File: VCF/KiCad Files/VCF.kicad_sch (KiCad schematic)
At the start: 64 parts, among them J1 AUDIO_IN, J2 CV1, J3 CV2, J4 AUDIO_OUT, J5 Conn_02x05_Odd_Even, J6 Conn_01x05_Male, J7 Conn_01x05_Female, J8 Conn_01x08_Male, J9 Conn_01x08_Female, SW1 SW_DPDT_x2, U1 TL074, U2 TL074

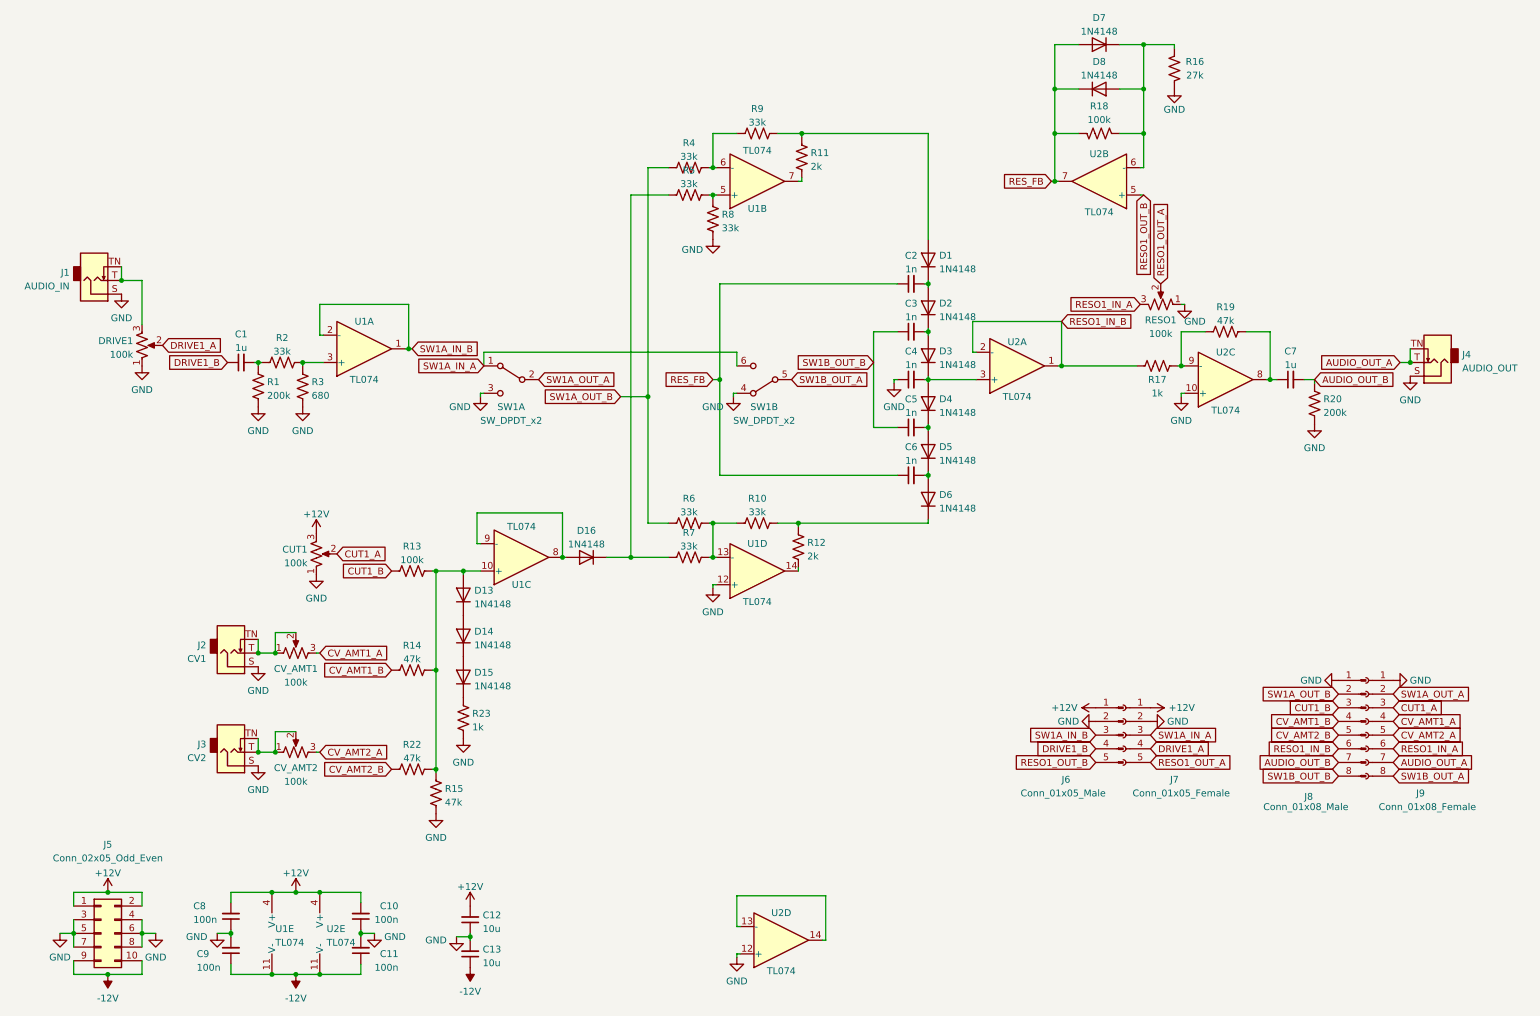
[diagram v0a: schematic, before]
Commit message: Corrected PCB
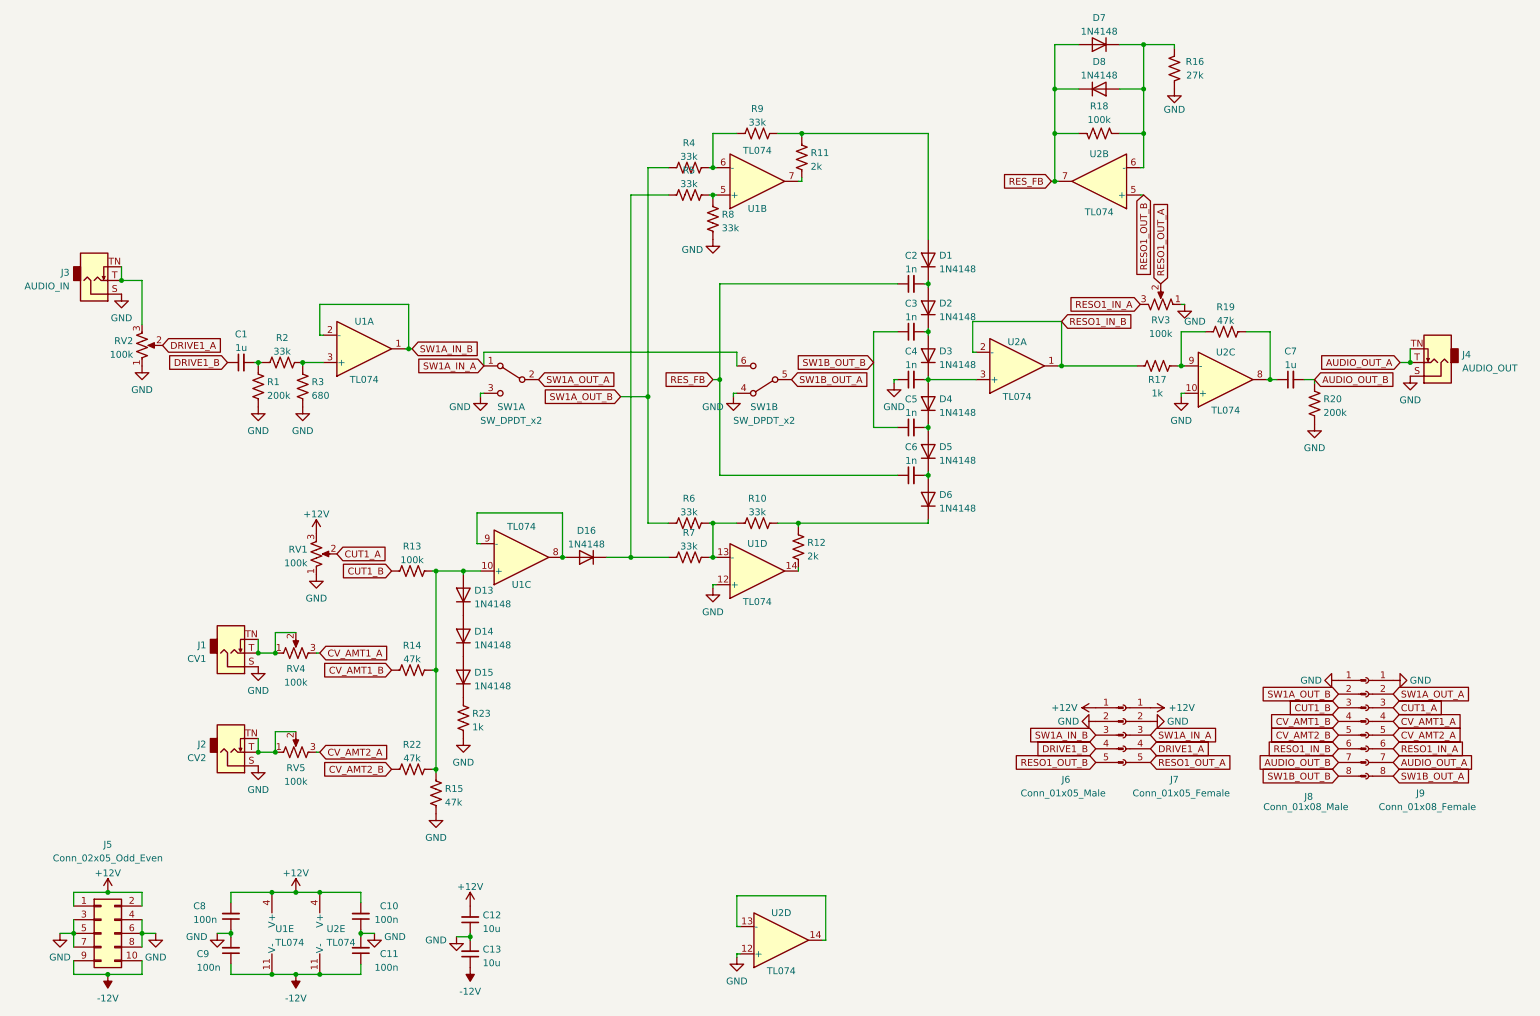
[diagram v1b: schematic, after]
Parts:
- renumbered J2 to J1, J3 to J2, J1 to J3, CUT1 to RV1, DRIVE1 to RV2, RESO1 to RV3, CV_AMT1 to RV4, CV_AMT2 to RV5
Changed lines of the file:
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@@
   (symbol (lib_id "Device:R_Potentiometer_US") (at 30.48 74.295 0) (mirror x) (unit 1)
     (in_bom yes) (on_board yes)
-    (property "Reference" "DRIVE1" (id 0) (at 28.829 73.4603 0)
+    (property "Reference" "RV2" (id 0) (at 28.829 73.4603 0)
       (effects (font (size 1.27 1.27)) (justify right))
     )
@@
   (symbol (lib_id "Device:R_Potentiometer_US") (at 62.865 113.03 0) (mirror x) (unit 1)
     (in_bom yes) (on_board yes) (fields_autoplaced)
-    (property "Reference" "CUT1" (id 0) (at 61.214 112.1953 0)
-      (effects (font (size 1.27 1.27)) (justify right))
-    )
-    (property "Value" "100k" (id 1) (at 61.214 114.7322 0)
+    (property "Reference" "RV1" (id 0) (at 61.2141 112.1953 0)
+      (effects (font (size 1.27 1.27)) (justify right))
+    )
+    (property "Value" "100k" (id 1) (at 61.2141 114.7322 0)
       (effects (font (size 1.27 1.27)) (justify right))
     )
@@
   (symbol (lib_id "Connector:AudioJack2_SwitchT") (at 21.59 62.23 0) (mirror x) (unit 1)
     (in_bom yes) (on_board yes) (fields_autoplaced)
-    (property "Reference" "J1" (id 0) (at 17.0181 60.7603 0)
+    (property "Reference" "J3" (id 0) (at 17.0181 60.7603 0)
       (effects (font (size 1.27 1.27)) (justify right))
     )
@@
   (symbol (lib_id "Device:R_Potentiometer_US") (at 59.055 149.86 90) (unit 1)
     (in_bom yes) (on_board yes) (fields_autoplaced)
-    (property "Reference" "CV_AMT2" (id 0) (at 59.055 152.7794 90))
+    (property "Reference" "RV5" (id 0) (at 59.055 152.7794 90))
     (property "Value" "100k" (id 1) (at 59.055 155.3163 90))
     (property "Footprint" "1_CUSTOM:Potentiometer_Alpha_Metal" (id 2) (at 59.055 149.86 0)
@@
   (symbol (lib_id "Device:R_Potentiometer_US") (at 219.71 66.675 270) (mirror x) (unit 1)
     (in_bom yes) (on_board yes) (fields_autoplaced)
-    (property "Reference" "RESO1" (id 0) (at 219.71 69.5944 90))
+    (property "Reference" "RV3" (id 0) (at 219.71 69.5944 90))
     (property "Value" "100k" (id 1) (at 219.71 72.1313 90))
     (property "Footprint" "1_CUSTOM:Potentiometer_Alpha_Metal" (id 2) (at 219.71 66.675 0)
@@
   (symbol (lib_id "Connector:AudioJack2_SwitchT") (at 46.99 149.86 0) (mirror x) (unit 1)
     (in_bom yes) (on_board yes) (fields_autoplaced)
-    (property "Reference" "J3" (id 0) (at 42.4181 148.3903 0)
+    (property "Reference" "J2" (id 0) (at 42.4181 148.3903 0)
       (effects (font (size 1.27 1.27)) (justify right))
     )
@@
   (symbol (lib_id "Connector:AudioJack2_SwitchT") (at 46.99 131.445 0) (mirror x) (unit 1)
     (in_bom yes) (on_board yes) (fields_autoplaced)
-    (property "Reference" "J2" (id 0) (at 42.4181 129.9753 0)
+    (property "Reference" "J1" (id 0) (at 42.4181 129.9753 0)
       (effects (font (size 1.27 1.27)) (justify right))
     )
@@
   (symbol (lib_id "Device:R_Potentiometer_US") (at 59.055 131.445 90) (unit 1)
     (in_bom yes) (on_board yes) (fields_autoplaced)
-    (property "Reference" "CV_AMT1" (id 0) (at 59.055 134.3644 90))
+    (property "Reference" "RV4" (id 0) (at 59.055 134.3644 90))
     (property "Value" "100k" (id 1) (at 59.055 136.9013 90))
     (property "Footprint" "1_CUSTOM:Potentiometer_Alpha_Metal" (id 2) (at 59.055 131.445 0)
@@
       (reference "C13") (unit 1) (value "10u") (footprint "Capacitor_SMD:CP_Elec_5x5.4")
     )
-    (path "/381f4c0d-9543-4911-8da2-34e065cd7bd2"
-      (reference "CUT1") (unit 1) (value "100k") (footprint "1_CUSTOM:Potentiometer_Alpha_Metal")
-    )
-    (path "/df147264-04c5-448c-aef7-d922329bd23c"
-      (reference "CV_AMT1") (unit 1) (value "100k") (footprint "1_CUSTOM:Potentiometer_Alpha_Metal")
-    )
-    (path "/709215a6-0e79-4071-81e0-fccd8f17331b"
-      (reference "CV_AMT2") (unit 1) (value "100k") (footprint "1_CUSTOM:Potentiometer_Alpha_Metal")
-    )
     (path "/5dde91f8-ddf6-45eb-a0db-b81980ac66ac"
       (reference "D1") (unit 1) (value "1N4148") (footprint "Diode_SMD:D_SOD-323_HandSoldering")
@@
       (reference "D16") (unit 1) (value "1N4148") (footprint "Diode_SMD:D_SOD-323_HandSoldering")
     )
-    (path "/2163dbd0-9c20-4f43-b9c8-b7932544841e"
-      (reference "DRIVE1") (unit 1) (value "100k") (footprint "1_CUSTOM:Potentiometer_Alpha_Metal")
+    (path "/cf157f36-01a1-4d50-b942-70f5c7e8db53"
+      (reference "J1") (unit 1) (value "CV1") (footprint "1_CUSTOM:Jack_3.5mm_QingPu_WQP-PJ398SM_Vertical_CircularHoles_Compact")
+    )
+    (path "/8e3c0888-34bb-466d-9c9f-31b726e28c32"
+      (reference "J2") (unit 1) (value "CV2") (footprint "1_CUSTOM:Jack_3.5mm_QingPu_WQP-PJ398SM_Vertical_CircularHoles_Compact")
     )
     (path "/5c1b3168-0f23-417d-aad7-0902d6085c21"
-      (reference "J1") (unit 1) (value "AUDIO_IN") (footprint "1_CUSTOM:Jack_3.5mm_QingPu_WQP-PJ398SM_Vertical_CircularHoles_Compact")
-    )
-    (path "/cf157f36-01a1-4d50-b942-70f5c7e8db53"
-      (reference "J2") (unit 1) (value "CV1") (footprint "1_CUSTOM:Jack_3.5mm_QingPu_WQP-PJ398SM_Vertical_CircularHoles_Compact")
-    )
-    (path "/8e3c0888-34bb-466d-9c9f-31b726e28c32"
-      (reference "J3") (unit 1) (value "CV2") (footprint "1_CUSTOM:Jack_3.5mm_QingPu_WQP-PJ398SM_Vertical_CircularHoles_Compact")
+      (reference "J3") (unit 1) (value "AUDIO_IN") (footprint "1_CUSTOM:Jack_3.5mm_QingPu_WQP-PJ398SM_Vertical_CircularHoles_Compact")
     )
     (path "/49ae8030-f3a5-42e5-a910-2db8c6cc87f3"
@@
       (reference "R23") (unit 1) (value "1k") (footprint "Resistor_SMD:R_0603_1608Metric_Pad0.98x0.95mm_HandSolder")
     )
+    (path "/381f4c0d-9543-4911-8da2-34e065cd7bd2"
+      (reference "RV1") (unit 1) (value "100k") (footprint "1_CUSTOM:Potentiometer_Alpha_Metal")
+    )
+    (path "/2163dbd0-9c20-4f43-b9c8-b7932544841e"
+      (reference "RV2") (unit 1) (value "100k") (footprint "1_CUSTOM:Potentiometer_Alpha_Metal")
+    )
     (path "/746d8b00-b8bf-43c7-aa7a-571bd4239b35"
-      (reference "RESO1") (unit 1) (value "100k") (footprint "1_CUSTOM:Potentiometer_Alpha_Metal")
+      (reference "RV3") (unit 1) (value "100k") (footprint "1_CUSTOM:Potentiometer_Alpha_Metal")
+    )
+    (path "/df147264-04c5-448c-aef7-d922329bd23c"
+      (reference "RV4") (unit 1) (value "100k") (footprint "1_CUSTOM:Potentiometer_Alpha_Metal")
+    )
+    (path "/709215a6-0e79-4071-81e0-fccd8f17331b"
+      (reference "RV5") (unit 1) (value "100k") (footprint "1_CUSTOM:Potentiometer_Alpha_Metal")
     )
     (path "/c2e3be15-ede1-4026-84c1-4e22811d1263"

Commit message: Cleaned up schematic
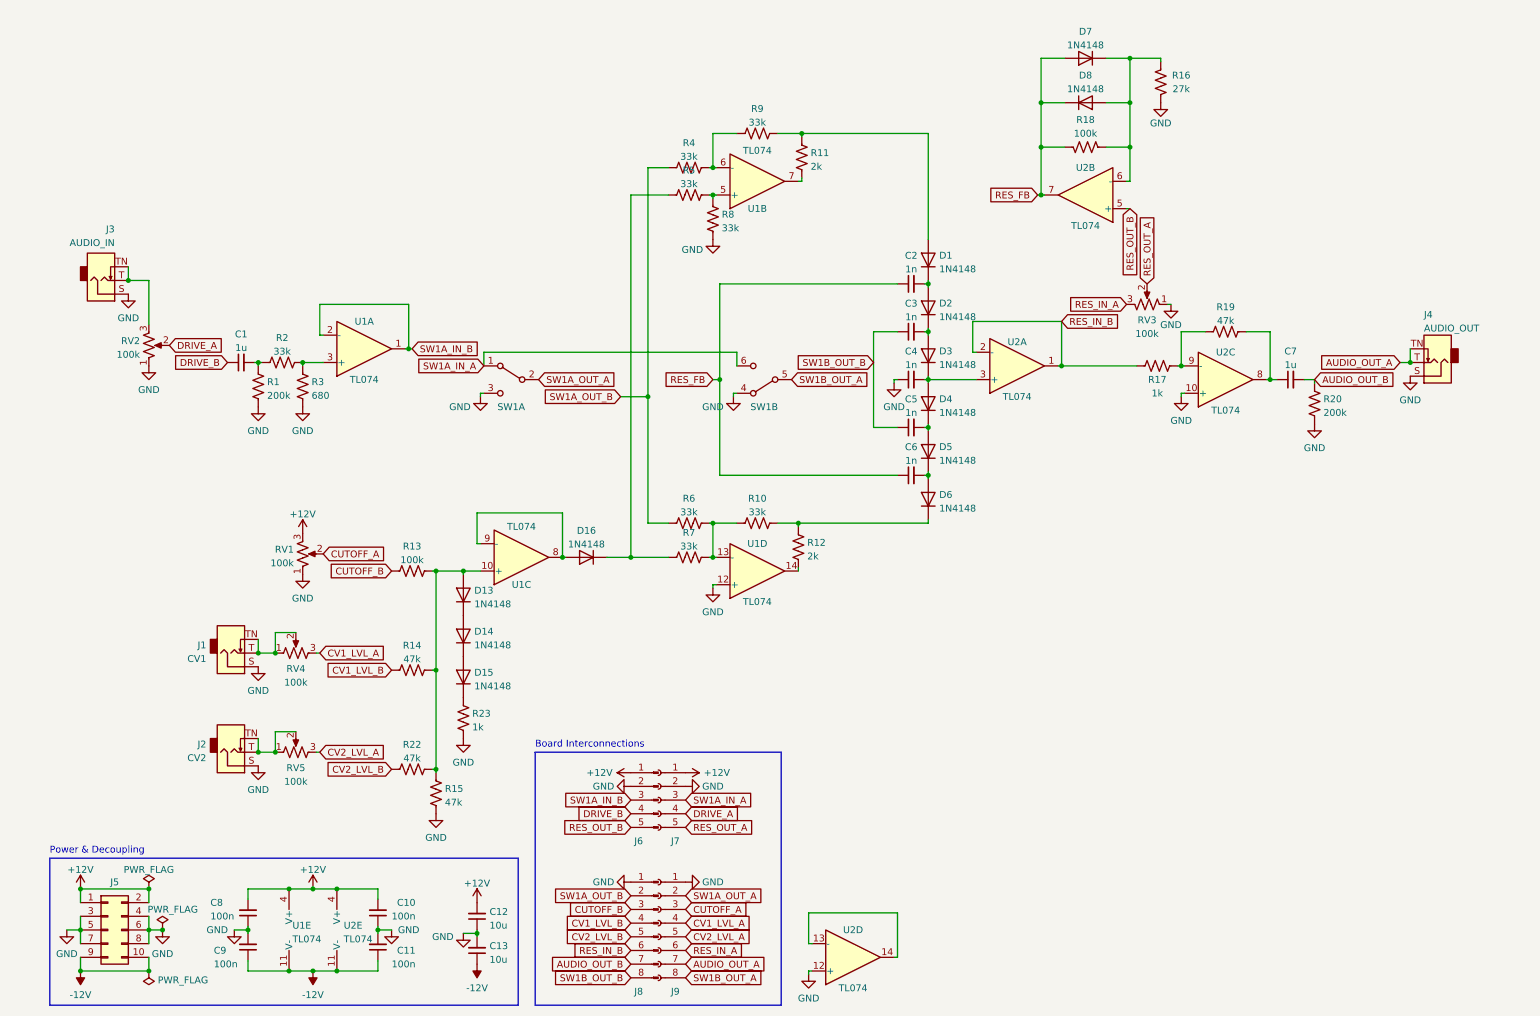
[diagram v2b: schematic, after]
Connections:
- net CUT1_A renamed CUTOFF_A
- net CUT1_B renamed CUTOFF_B
- net CV_AMT1_A renamed CV1_LVL_A
- net CV_AMT1_B renamed CV1_LVL_B
- net CV_AMT2_A renamed CV2_LVL_A
- net CV_AMT2_B renamed CV2_LVL_B
- net DRIVE1_A renamed DRIVE_A
- net DRIVE1_B renamed DRIVE_B
- net RESO1_IN_A renamed RES_IN_A
- net RESO1_IN_B renamed RES_IN_B
- net RESO1_OUT_A renamed RES_OUT_A
- net RESO1_OUT_B renamed RES_OUT_B
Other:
- note added: "Board Interconnections"
- note added: "Power & Decoupling"
- moved on the sheet: C10, C11, C12, C13, C8, C9, D7, D8, J3, J5, J6, J7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
